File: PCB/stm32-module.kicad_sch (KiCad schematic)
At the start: 24 parts, among them J1 Left, J2 Right

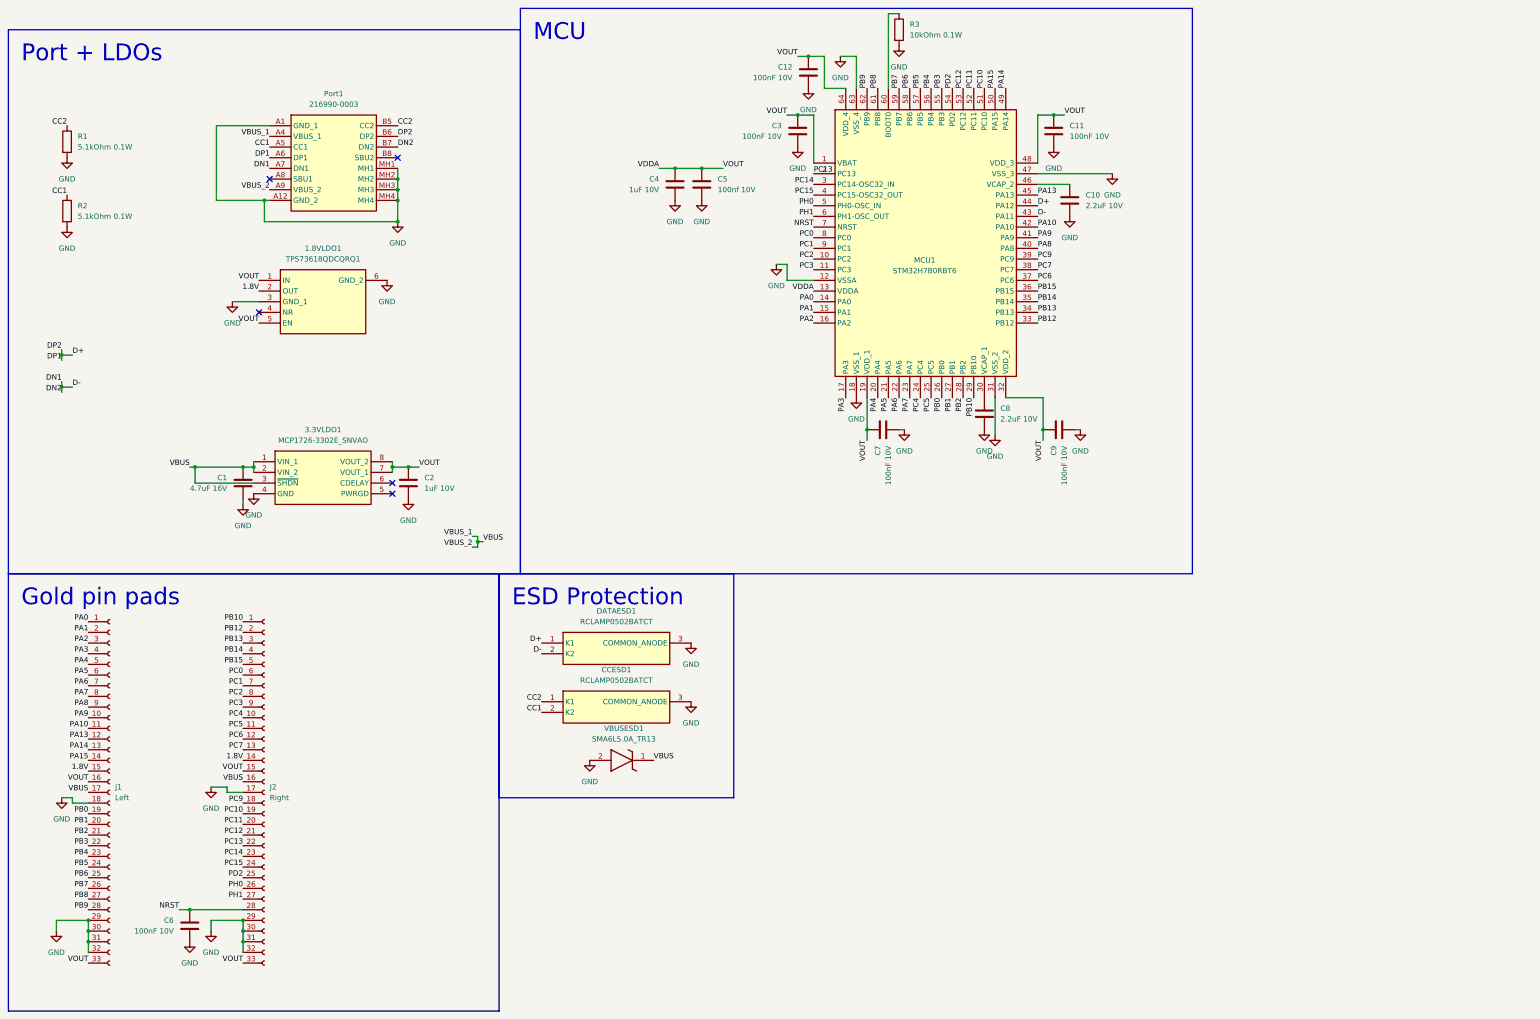
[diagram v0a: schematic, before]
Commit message: Added images to rom, also rerouted everything
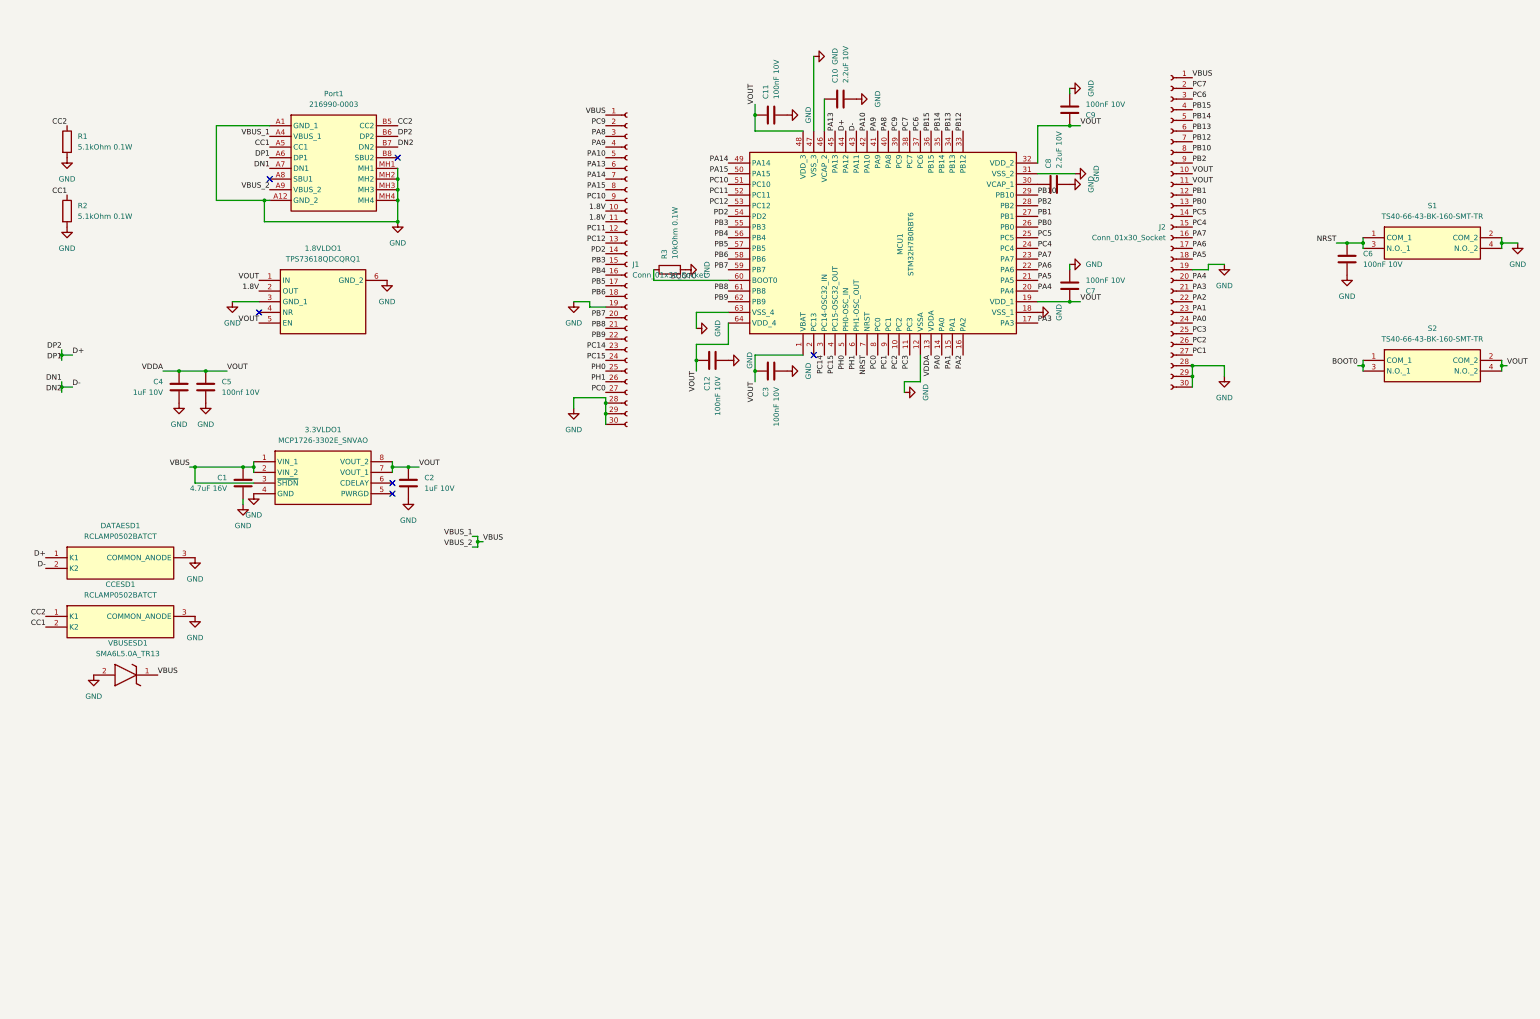
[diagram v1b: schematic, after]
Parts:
- removed J1: Left, symbol REQUIRED:Conn_01x33_Socket
- removed J2: Right, Connector_PinSocket_2.54mm:PinSocket_1x33_P2.54mm_Vertical, symbol REQUIRED:Conn_01x33_Socket
- added J1, J2: Conn_01x30_Socket, Connector_PinSocket_2.54mm:PinSocket_1x30_P2.54mm_Vertical, symbol REQUIRED:Conn_01x30_Socket
- added S1, S2: TS40-66-43-BK-160-SMT-TR, SamacSys_Parts:TS406643BK160SMTTR, symbol REQUIRED:TS40-66-43-BK-160-SMT-TR
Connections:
- net 1.8V: now also J1.10 (Pin_10), J1.11 (Pin_11)
- net GND: now also J1.19 (Pin_19), J1.28 (Pin_28), J1.29 (Pin_29), J1.30 (Pin_30), J2.19 (Pin_19), J2.28 (Pin_28), J2.29 (Pin_29), J2.30 (Pin_30), S1.2 (COM_2), S1.4 (N.O._2)
- net NRST: now also S1.1 (COM_1), S1.3 (N.O._1)
- net PA0: now also J2.24 (Pin_24)
- net PA1: now also J2.23 (Pin_23)
- net PA10: now also J1.5 (Pin_5)
- net PA13: now also J1.6 (Pin_6)
- net PA14: now also J1.7 (Pin_7)
- net PA15: now also J1.8 (Pin_8)
- net PA2: now also J2.22 (Pin_22)
- net PA3: now also J2.21 (Pin_21)
- net PA4: now also J2.20 (Pin_20)
- net PA5: now also J2.18 (Pin_18)
- net PA6: now also J2.17 (Pin_17)
- net PA7: now also J2.16 (Pin_16)
- net PA8: now also J1.3 (Pin_3)
- net PA9: now also J1.4 (Pin_4)
- net PB0: now also J2.13 (Pin_13)
- net PB1: now also J2.12 (Pin_12)
- net PB10: now also J2.8 (Pin_8)
- net PB12: now also J2.7 (Pin_7)
- net PB13: now also J2.6 (Pin_6)
- net PB14: now also J2.5 (Pin_5)
- net PB15: now also J2.4 (Pin_4)
- net PB2: now also J2.9 (Pin_9)
- net PB3: now also J1.15 (Pin_15)
- net PB4: now also J1.16 (Pin_16)
- net PB5: now also J1.17 (Pin_17)
- net PB6: now also J1.18 (Pin_18)
- net PB7: now also J1.20 (Pin_20)
- net PB8: now also J1.21 (Pin_21)
- net PB9: now also J1.22 (Pin_22)
- net PC0: now also J1.27 (Pin_27)
- net PC1: now also J2.27 (Pin_27)
- net PC10: now also J1.9 (Pin_9)
- net PC11: now also J1.12 (Pin_12)
- net PC12: now also J1.13 (Pin_13)
- net PC14: now also J1.23 (Pin_23)
- net PC15: now also J1.24 (Pin_24)
- net PC2: now also J2.26 (Pin_26)
- net PC3: now also J2.25 (Pin_25)
- net PC4: now also J2.15 (Pin_15)
- net PC5: now also J2.14 (Pin_14)
- net PC6: now also J2.3 (Pin_3)
- net PC7: now also J2.2 (Pin_2)
- net PC9: now also J1.2 (Pin_2)
- net PD2: now also J1.14 (Pin_14)
- net PH0: now also J1.25 (Pin_25)
- net PH1: now also J1.26 (Pin_26)
- net VBUS: now also J1.1 (Pin_1), J2.1 (Pin_1)
- net VDDA: now also J2.10 (Pin_10), J2.11 (Pin_11), S2.2 (COM_2), S2.4 (N.O._2)
- net BOOT0: now reaches MCU1.60 (BOOT0), R3.1
- net BOOT0: now also S2.1 (COM_1), S2.3 (N.O._1)
- net PC13: no longer names the net of MCU1.2 (PC13)
- no-connect marks 5 -> 6
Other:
- moved on the sheet: C10, C11, C12, C3, C4, C5, C7, C8, C9, CCESD1, DATAESD1, MCU1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

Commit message: Changed readme, pcb and schematic to reflect different connector chosen due to availability
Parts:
- removed Port1: 216990-0003, SamacSys_Parts:2169900003, symbol REQUIRED:216990-0003
- added USB1: ~, REQUIRED:conn, symbol REQUIRED:TYPE-C 16PIN 2MD(073)
- S1, S2: value TS40-66-43-BK-160-SMT-TR -> SHOU HAN TS6643TP 250gf 009; Manufacturer_Name Same Sky -> SHOU HAN; Manufacturer_Part_Number TS40-66-43-BK-160-SMT-TR -> TS6643TP 250gf 009
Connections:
- net CC1: now also USB1.4 (CC1)
- net CC2: now also USB1.10 (CC2)
- net D+: now also USB1.6 (DP1), USB1.8 (DP2)
- net D-: now also USB1.5 (DN2), USB1.7 (DN1)
- net GND: now also USB1.1 (GND), USB1.12 (GND), USB1.13 (SHELL), USB1.14 (SHELL)
- net VBUS: now also USB1.11 (VBUS), USB1.2 (VBUS)

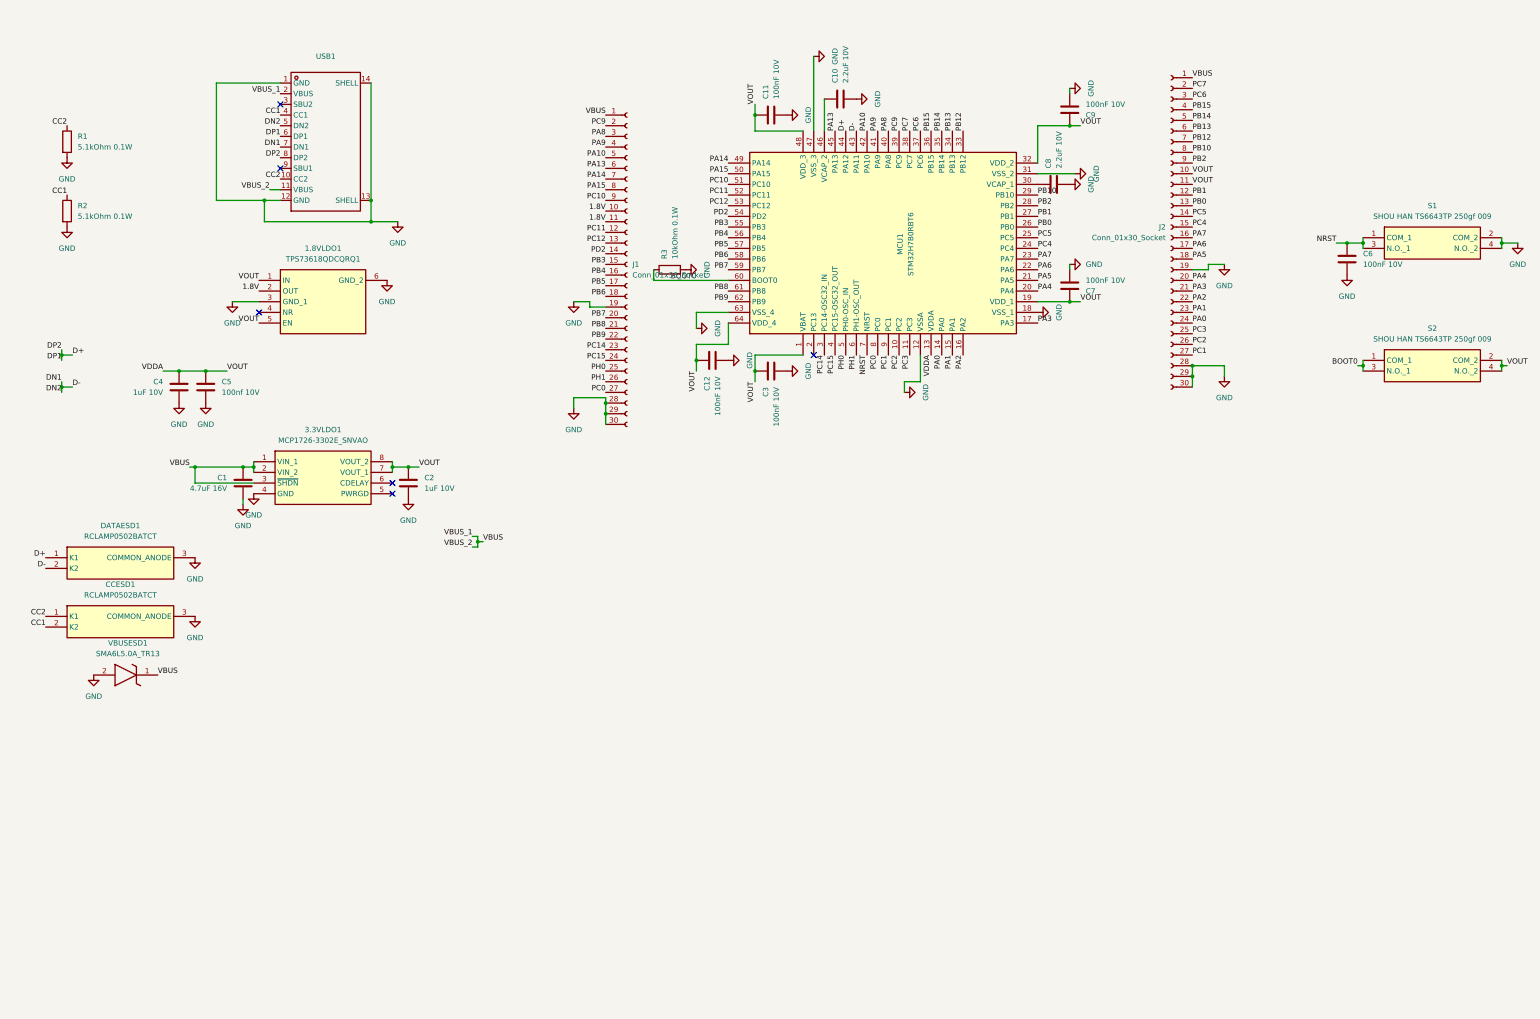
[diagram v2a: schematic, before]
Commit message: Added connector footprint with 3d model
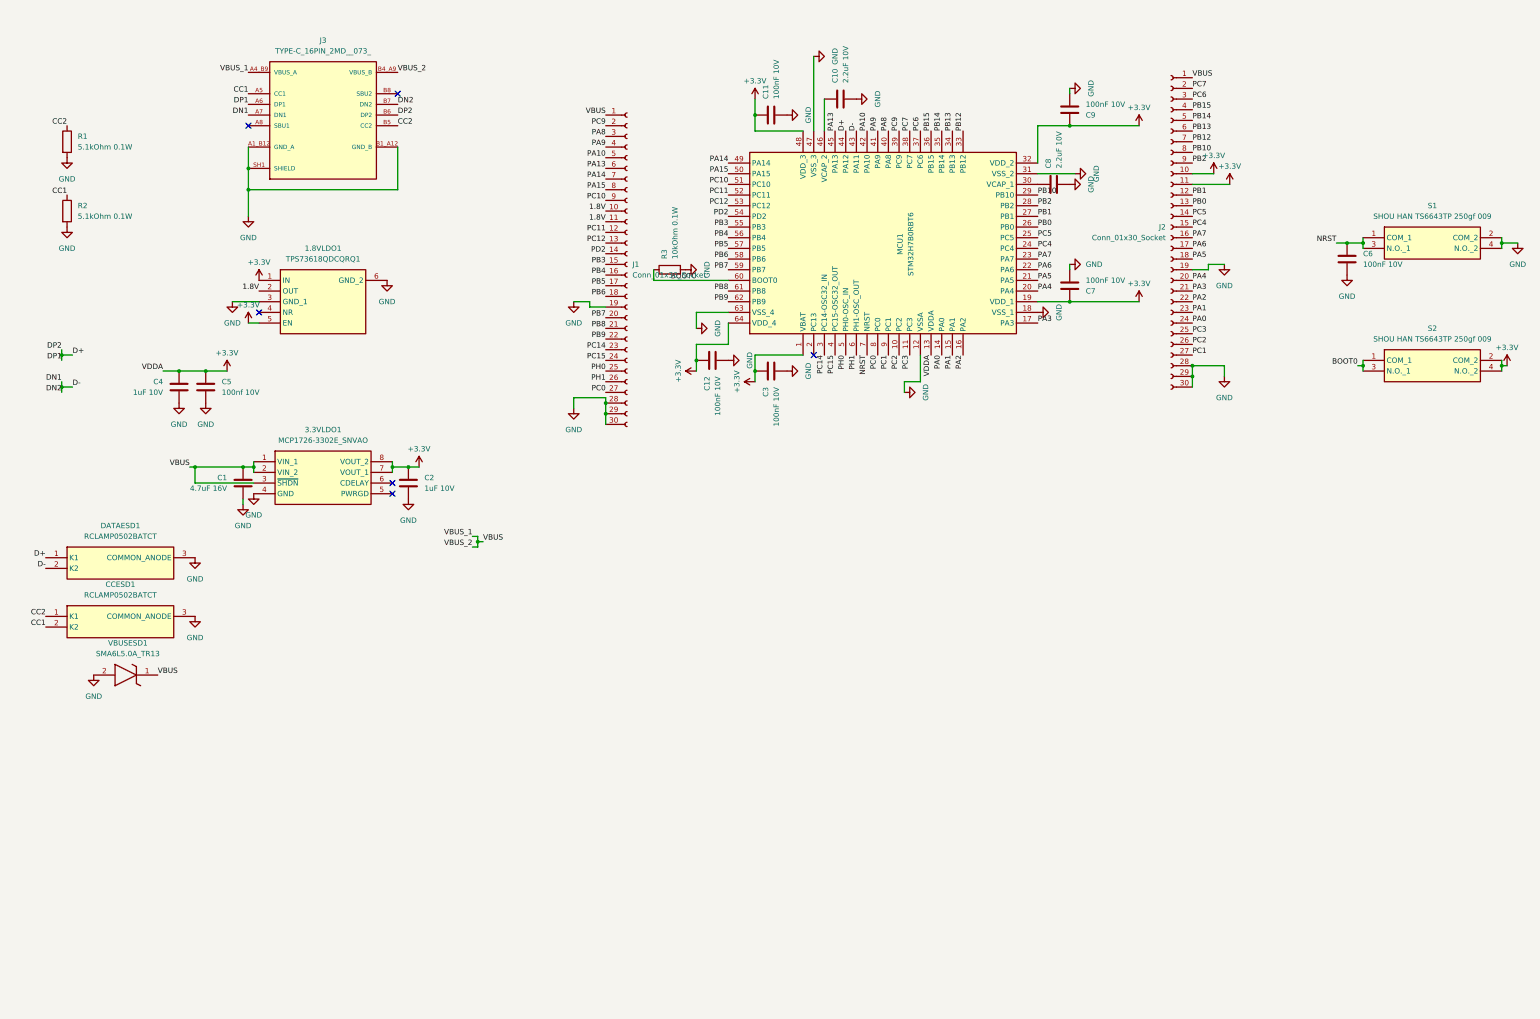
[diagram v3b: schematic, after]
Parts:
- removed USB1: ~, REQUIRED:conn, symbol REQUIRED:TYPE-C 16PIN 2MD(073)
- added J3: TYPE-C_16PIN_2MD__073_, TYPE-C_16PIN_2MD__073_:SHOUHAN_TYPE-C_16PIN_2MD__073_, symbol REQUIRED:TYPE-C_16PIN_2MD__073_
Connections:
- net CC1: now also J3.A5 (CC1)
- net CC2: now also J3.B5 (CC2)
- net D+: now also J3.A6 (DP1), J3.B6 (DP2)
- net D-: now also J3.A7 (DN1), J3.B7 (DN2)
- net GND: now also J3.A1_B12 (GND_A), J3.B1_A12 (GND_B), J3.SH1 (SHIELD), J3.SH2 (SHIELD), J3.SH3 (SHIELD), J3.SH4 (SHIELD)
- net VBUS: now also J3.A4_B9 (VBUS_A), J3.B4_A9 (VBUS_B)
- net VDDA renamed +3.3V

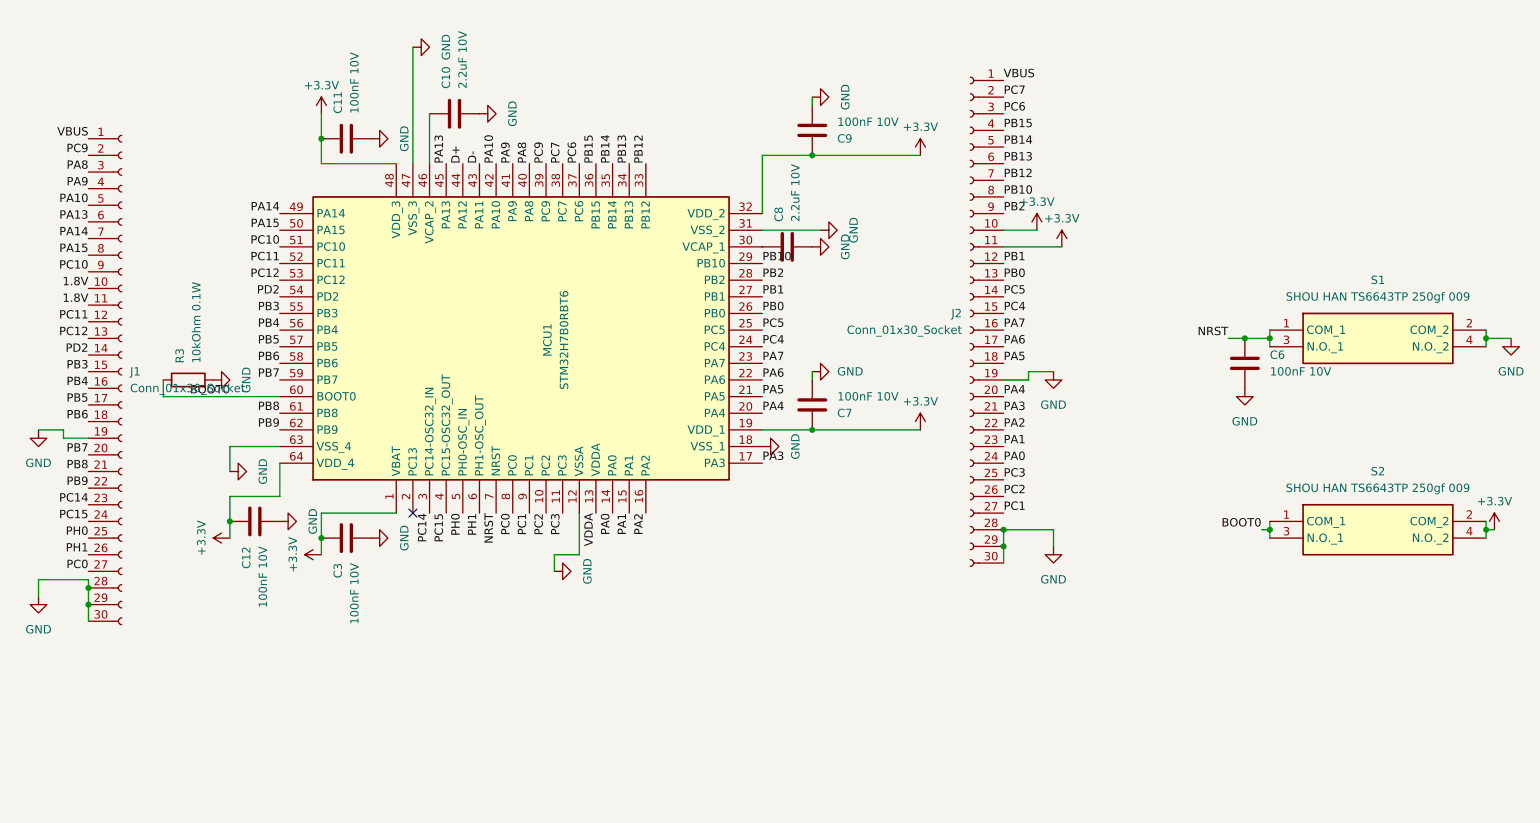
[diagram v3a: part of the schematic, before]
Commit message: Corrected button wiring
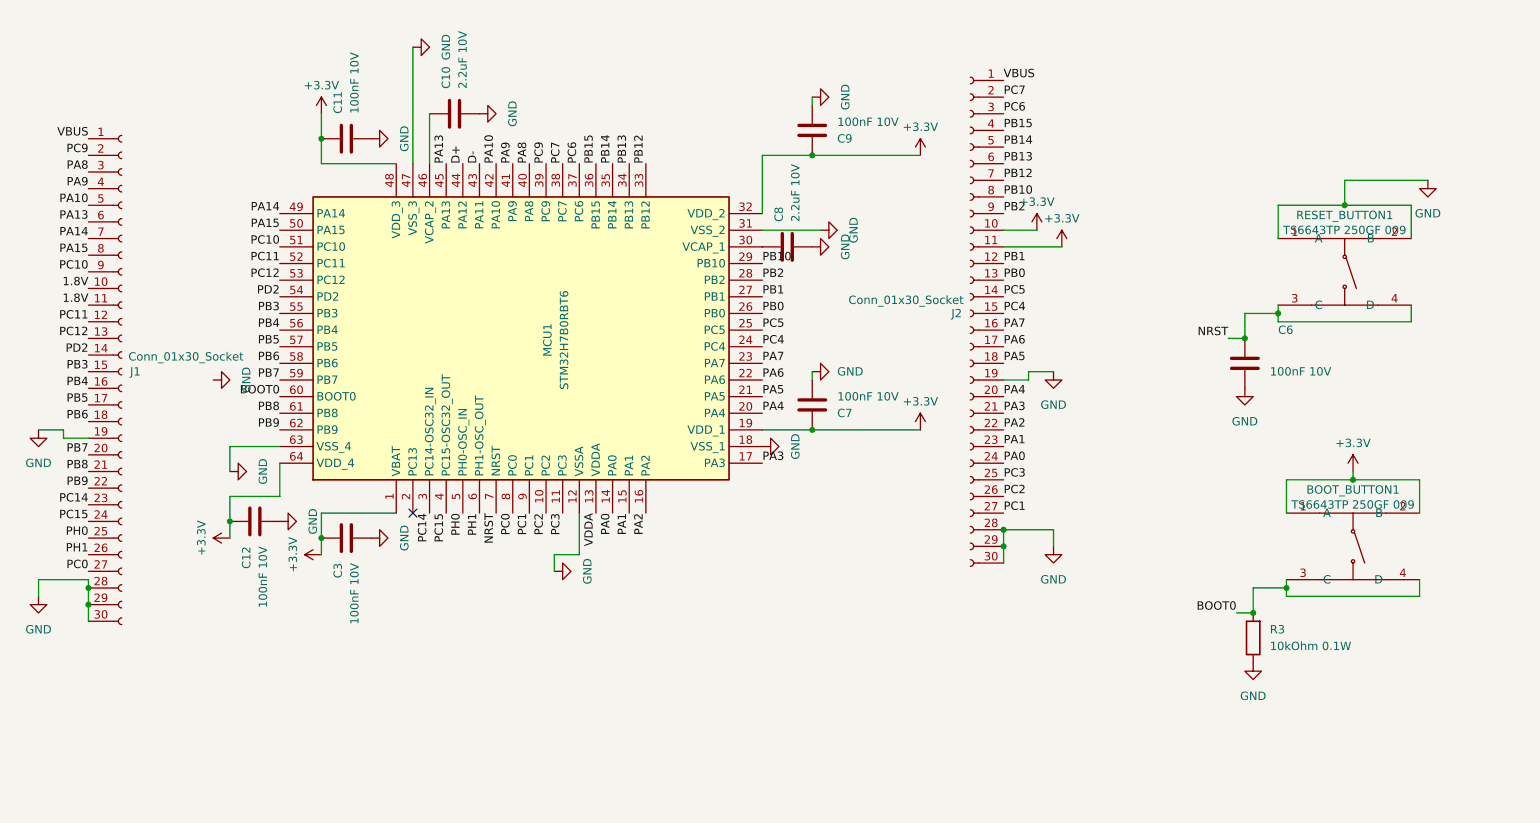
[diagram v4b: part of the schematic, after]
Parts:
- removed S1, S2: SHOU HAN TS6643TP 250gf 009, SamacSys_Parts:TS406643BK160SMTTR, symbol REQUIRED:TS40-66-43-BK-160-SMT-TR
- added BOOT_BUTTON1, RESET_BUTTON1: TS6643TP 250GF 009, easyeda2kicad:SW-SMD_4P-L6.2-W6.0-P4.50-LS9.0, symbol REQUIRED:TS6643TP250GF009
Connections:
- net +3.3V: now also BOOT_BUTTON1.1 (A), BOOT_BUTTON1.2 (B)
- net BOOT0: now also R3.2, BOOT_BUTTON1.3 (C), BOOT_BUTTON1.4 (D); no longer R3.1
- net GND: now also R3.1, RESET_BUTTON1.1 (A), RESET_BUTTON1.2 (B); no longer R3.2
- net NRST: now also RESET_BUTTON1.3 (C), RESET_BUTTON1.4 (D)
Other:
- moved on the sheet: R3
